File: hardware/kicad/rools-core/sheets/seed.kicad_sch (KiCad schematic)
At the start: 3 parts, among them J7 J_TOP_MAIN, J8 J_BOT_MAIN

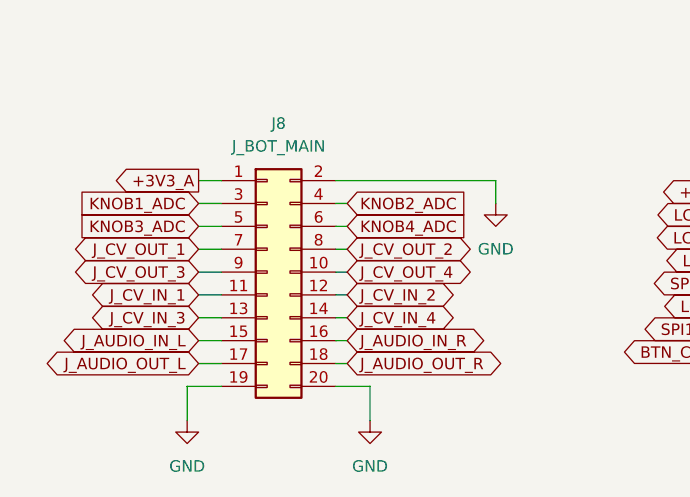
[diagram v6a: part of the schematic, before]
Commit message: Remove Patch reference assets and continue Core PCB routing.
Drop imported Patch symbols, local display footprint, and stale BOM CSV while advancing layout and schematic interconnects.

Co-authored-by: Cursor <cursoragent@cursor.com>
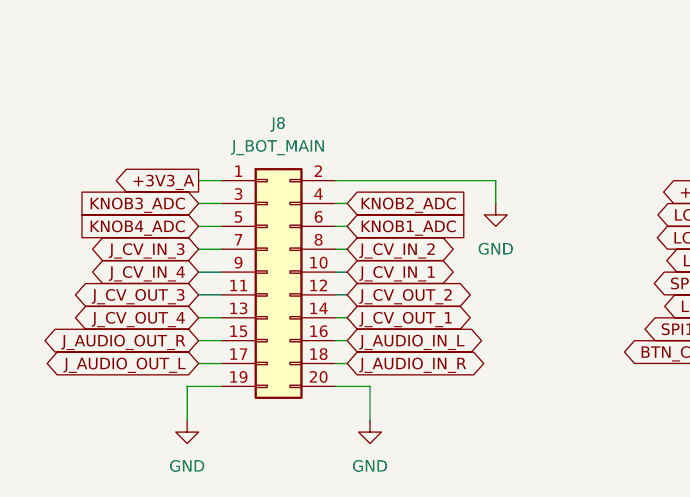
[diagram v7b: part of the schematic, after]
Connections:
- net J_AUDIO_IN_L: now also J8.16 (Pin_16); no longer J8.15 (Pin_15)
- net J_AUDIO_IN_R: now also J8.18 (Pin_18); no longer J8.16 (Pin_16)
- net J_AUDIO_OUT_R: now also J8.15 (Pin_15); no longer J8.18 (Pin_18)
- net J_CV_IN_1: now also J8.10 (Pin_10); no longer J8.11 (Pin_11)
- net J_CV_IN_2: now also J8.8 (Pin_8); no longer J8.12 (Pin_12)
- net J_CV_IN_3: now also J8.7 (Pin_7); no longer J8.13 (Pin_13)
- net J_CV_IN_4: now also J8.9 (Pin_9); no longer J8.14 (Pin_14)
- net J_CV_OUT_1: now also J8.14 (Pin_14); no longer J8.7 (Pin_7)
- net J_CV_OUT_2: now also J8.12 (Pin_12); no longer J8.8 (Pin_8)
- net J_CV_OUT_3: now also J8.11 (Pin_11); no longer J8.9 (Pin_9)
- net J_CV_OUT_4: now also J8.13 (Pin_13); no longer J8.10 (Pin_10)
- net KNOB1_ADC: now also J8.6 (Pin_6); no longer J8.3 (Pin_3)
- net KNOB3_ADC: now also J8.3 (Pin_3); no longer J8.5 (Pin_5)
- net KNOB4_ADC: now also J8.5 (Pin_5); no longer J8.6 (Pin_6)
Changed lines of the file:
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@@
 	(global_label "KNOB4_ADC"
 		(shape input)
-		(at 116.84 125.73 0)
-		(fields_autoplaced yes)
-		(effects
-			(font
-				(size 1.27 1.27)
-			)
-			(justify left)
-		)
-		(property "Intersheetrefs" "${INTERSHEET_REFS}"
-			(at 130.927 125.73 0)
-			(hide yes)
-			(show_name no)
-			(do_not_autoplace no)
-			(effects
-				(font
-					(size 1.27 1.27)
-				)
-				(justify left)
+		(at 100.33 125.73 180)
+		(fields_autoplaced yes)
+		(effects
+			(font
+				(size 1.27 1.27)
+			)
+			(justify right)
+		)
+		(property "Intersheetrefs" "${INTERSHEET_REFS}"
+			(at 86.243 125.73 0)
+			(hide yes)
+			(show_name no)
+			(do_not_autoplace no)
+			(effects
+				(font
+					(size 1.27 1.27)
+				)
+				(justify right)
 			)
 		)
@@
 	(global_label "J_AUDIO_IN_R"
 		(shape bidirectional)
-		(at 116.84 138.43 0)
-		(fields_autoplaced yes)
-		(effects
-			(font
-				(size 1.27 1.27)
-			)
-			(justify left)
-		)
-		(property "Intersheetrefs" "${INTERSHEET_REFS}"
-			(at 133.6364 138.43 0)
+		(at 116.84 140.97 0)
+		(fields_autoplaced yes)
+		(effects
+			(font
+				(size 1.27 1.27)
+			)
+			(justify left)
+		)
+		(property "Intersheetrefs" "${INTERSHEET_REFS}"
+			(at 133.6364 140.97 0)
 			(hide yes)
 			(show_name no)
@@
 	(global_label "J_CV_OUT_1"
 		(shape bidirectional)
-		(at 100.33 128.27 180)
-		(fields_autoplaced yes)
-		(effects
-			(font
-				(size 1.27 1.27)
-			)
-			(justify right)
-		)
-		(property "Intersheetrefs" "${INTERSHEET_REFS}"
-			(at 85.1666 128.27 0)
-			(hide yes)
-			(show_name no)
-			(do_not_autoplace no)
-			(effects
-				(font
-					(size 1.27 1.27)
-				)
-				(justify right)
+		(at 116.84 135.89 0)
+		(fields_autoplaced yes)
+		(effects
+			(font
+				(size 1.27 1.27)
+			)
+			(justify left)
+		)
+		(property "Intersheetrefs" "${INTERSHEET_REFS}"
+			(at 132.0034 135.89 0)
+			(hide yes)
+			(show_name no)
+			(do_not_autoplace no)
+			(effects
+				(font
+					(size 1.27 1.27)
+				)
+				(justify left)
 			)
 		)
@@
 	(global_label "J_CV_IN_1"
 		(shape bidirectional)
-		(at 100.33 133.35 180)
-		(fields_autoplaced yes)
-		(effects
-			(font
-				(size 1.27 1.27)
-			)
-			(justify right)
-		)
-		(property "Intersheetrefs" "${INTERSHEET_REFS}"
-			(at 86.8599 133.35 0)
-			(hide yes)
-			(show_name no)
-			(do_not_autoplace no)
-			(effects
-				(font
-					(size 1.27 1.27)
-				)
-				(justify right)
+		(at 116.84 130.81 0)
+		(fields_autoplaced yes)
+		(effects
+			(font
+				(size 1.27 1.27)
+			)
+			(justify left)
+		)
+		(property "Intersheetrefs" "${INTERSHEET_REFS}"
+			(at 130.3101 130.81 0)
+			(hide yes)
+			(show_name no)
+			(do_not_autoplace no)
+			(effects
+				(font
+					(size 1.27 1.27)
+				)
+				(justify left)
 			)
 		)
@@
 	(global_label "J_AUDIO_IN_L"
 		(shape bidirectional)
-		(at 100.33 138.43 180)
-		(fields_autoplaced yes)
-		(effects
-			(font
-				(size 1.27 1.27)
-			)
-			(justify right)
-		)
-		(property "Intersheetrefs" "${INTERSHEET_REFS}"
-			(at 83.7755 138.43 0)
-			(hide yes)
-			(show_name no)
-			(do_not_autoplace no)
-			(effects
-				(font
-					(size 1.27 1.27)
-				)
-				(justify right)
+		(at 116.84 138.43 0)
+		(fields_autoplaced yes)
+		(effects
+			(font
+				(size 1.27 1.27)
+			)
+			(justify left)
+		)
+		(property "Intersheetrefs" "${INTERSHEET_REFS}"
+			(at 133.3945 138.43 0)
+			(hide yes)
+			(show_name no)
+			(do_not_autoplace no)
+			(effects
+				(font
+					(size 1.27 1.27)
+				)
+				(justify left)
 			)
 		)
@@
 	(global_label "J_CV_IN_3"
 		(shape bidirectional)
-		(at 100.33 135.89 180)
-		(fields_autoplaced yes)
-		(effects
-			(font
-				(size 1.27 1.27)
-			)
-			(justify right)
-		)
-		(property "Intersheetrefs" "${INTERSHEET_REFS}"
-			(at 86.8599 135.89 0)
+		(at 100.33 128.27 180)
+		(fields_autoplaced yes)
+		(effects
+			(font
+				(size 1.27 1.27)
+			)
+			(justify right)
+		)
+		(property "Intersheetrefs" "${INTERSHEET_REFS}"
+			(at 86.8599 128.27 0)
 			(hide yes)
 			(show_name no)
@@
 	(global_label "J_CV_OUT_2"
 		(shape bidirectional)
-		(at 116.84 128.27 0)
-		(fields_autoplaced yes)
-		(effects
-			(font
-				(size 1.27 1.27)
-			)
-			(justify left)
-		)
-		(property "Intersheetrefs" "${INTERSHEET_REFS}"
-			(at 132.0034 128.27 0)
+		(at 116.84 133.35 0)
+		(fields_autoplaced yes)
+		(effects
+			(font
+				(size 1.27 1.27)
+			)
+			(justify left)
+		)
+		(property "Intersheetrefs" "${INTERSHEET_REFS}"
+			(at 132.0034 133.35 0)
 			(hide yes)
 			(show_name no)
@@
 	(global_label "J_CV_IN_2"
 		(shape bidirectional)
-		(at 116.84 133.35 0)
-		(fields_autoplaced yes)
-		(effects
-			(font
-				(size 1.27 1.27)
-			)
-			(justify left)
-		)
-		(property "Intersheetrefs" "${INTERSHEET_REFS}"
-			(at 130.3101 133.35 0)
+		(at 116.84 128.27 0)
+		(fields_autoplaced yes)
+		(effects
+			(font
+				(size 1.27 1.27)
+			)
+			(justify left)
+		)
+		(property "Intersheetrefs" "${INTERSHEET_REFS}"
+			(at 130.3101 128.27 0)
 			(hide yes)
 			(show_name no)
@@
 	(global_label "J_AUDIO_OUT_R"
 		(shape bidirectional)
-		(at 116.84 140.97 0)
-		(fields_autoplaced yes)
-		(effects
-			(font
-				(size 1.27 1.27)
-			)
-			(justify left)
-		)
-		(property "Intersheetrefs" "${INTERSHEET_REFS}"
-			(at 135.3297 140.97 0)
-			(hide yes)
-			(show_name no)
-			(do_not_autoplace no)
-			(effects
-				(font
-					(size 1.27 1.27)
-				)
-				(justify left)
+		(at 100.33 138.43 180)
+		(fields_autoplaced yes)
+		(effects
+			(font
+				(size 1.27 1.27)
+			)
+			(justify right)
+		)
+		(property "Intersheetrefs" "${INTERSHEET_REFS}"
+			(at 81.8403 138.43 0)
+			(hide yes)
+			(show_name no)
+			(do_not_autoplace no)
+			(effects
+				(font
+					(size 1.27 1.27)
+				)
+				(justify right)
 			)
 		)
@@
 	(global_label "KNOB3_ADC"
 		(shape input)
-		(at 100.33 125.73 180)
-		(fields_autoplaced yes)
-		(effects
-			(font
-				(size 1.27 1.27)
-			)
-			(justify right)
-		)
-		(property "Intersheetrefs" "${INTERSHEET_REFS}"
-			(at 86.243 125.73 0)
+		(at 100.33 123.19 180)
+		(fields_autoplaced yes)
+		(effects
+			(font
+				(size 1.27 1.27)
+			)
+			(justify right)
+		)
+		(property "Intersheetrefs" "${INTERSHEET_REFS}"
+			(at 86.243 123.19 0)
 			(hide yes)
 			(show_name no)
@@
 	(global_label "J_CV_OUT_4"
 		(shape bidirectional)
-		(at 116.84 130.81 0)
-		(fields_autoplaced yes)
-		(effects
-			(font
-				(size 1.27 1.27)
-			)
-			(justify left)
-		)
-		(property "Intersheetrefs" "${INTERSHEET_REFS}"
-			(at 132.0034 130.81 0)
-			(hide yes)
-			(show_name no)
-			(do_not_autoplace no)
-			(effects
-				(font
-					(size 1.27 1.27)
-				)
-				(justify left)
+		(at 100.33 135.89 180)
+		(fields_autoplaced yes)
+		(effects
+			(font
+				(size 1.27 1.27)
+			)
+			(justify right)
+		)
+		(property "Intersheetrefs" "${INTERSHEET_REFS}"
+			(at 85.1666 135.89 0)
+			(hide yes)
+			(show_name no)
+			(do_not_autoplace no)
+			(effects
+				(font
+					(size 1.27 1.27)
+				)
+				(justify right)
 			)
 		)
@@
 	(global_label "J_CV_IN_4"
 		(shape bidirectional)
-		(at 116.84 135.89 0)
-		(fields_autoplaced yes)
-		(effects
-			(font
-				(size 1.27 1.27)
-			)
-			(justify left)
-		)
-		(property "Intersheetrefs" "${INTERSHEET_REFS}"
-			(at 130.3101 135.89 0)
-			(hide yes)
-			(show_name no)
-			(do_not_autoplace no)
-			(effects
-				(font
-					(size 1.27 1.27)
-				)
-				(justify left)
+		(at 100.33 130.81 180)
+		(fields_autoplaced yes)
+		(effects
+			(font
+				(size 1.27 1.27)
+			)
+			(justify right)
+		)
+		(property "Intersheetrefs" "${INTERSHEET_REFS}"
+			(at 86.8599 130.81 0)
+			(hide yes)
+			(show_name no)
+			(do_not_autoplace no)
+			(effects
+				(font
+					(size 1.27 1.27)
+				)
+				(justify right)
 			)
 		)
@@
 	(global_label "KNOB1_ADC"
 		(shape input)
-		(at 100.33 123.19 180)
-		(fields_autoplaced yes)
-		(effects
-			(font
-				(size 1.27 1.27)
-			)
-			(justify right)
-		)
-		(property "Intersheetrefs" "${INTERSHEET_REFS}"
-			(at 86.243 123.19 0)
-			(hide yes)
-			(show_name no)
-			(do_not_autoplace no)
-			(effects
-				(font
-					(size 1.27 1.27)
-				)
-				(justify right)
+		(at 116.84 125.73 0)
+		(fields_autoplaced yes)
+		(effects
+			(font
+				(size 1.27 1.27)
+			)
+			(justify left)
+		)
+		(property "Intersheetrefs" "${INTERSHEET_REFS}"
+			(at 130.927 125.73 0)
+			(hide yes)
+			(show_name no)
+			(do_not_autoplace no)
+			(effects
+				(font
+					(size 1.27 1.27)
+				)
+				(justify left)
 			)
 		)
@@
 	(global_label "J_CV_OUT_3"
 		(shape bidirectional)
-		(at 100.33 130.81 180)
-		(fields_autoplaced yes)
-		(effects
-			(font
-				(size 1.27 1.27)
-			)
-			(justify right)
-		)
-		(property "Intersheetrefs" "${INTERSHEET_REFS}"
-			(at 85.1666 130.81 0)
-			(hide yes)
-			(show_name no)
+		(at 100.33 133.35 180)
+		(fields_autoplaced yes)
+		(effects
+			(font
+				(size 1.27 1.27)
+			)
+			(justify right)
+		)
+		(property "Intersheetrefs" "${INTERSHEET_REFS}"
+			(at 85.1666 133.35 0)
+			(hide yes)
+			(show_name no)

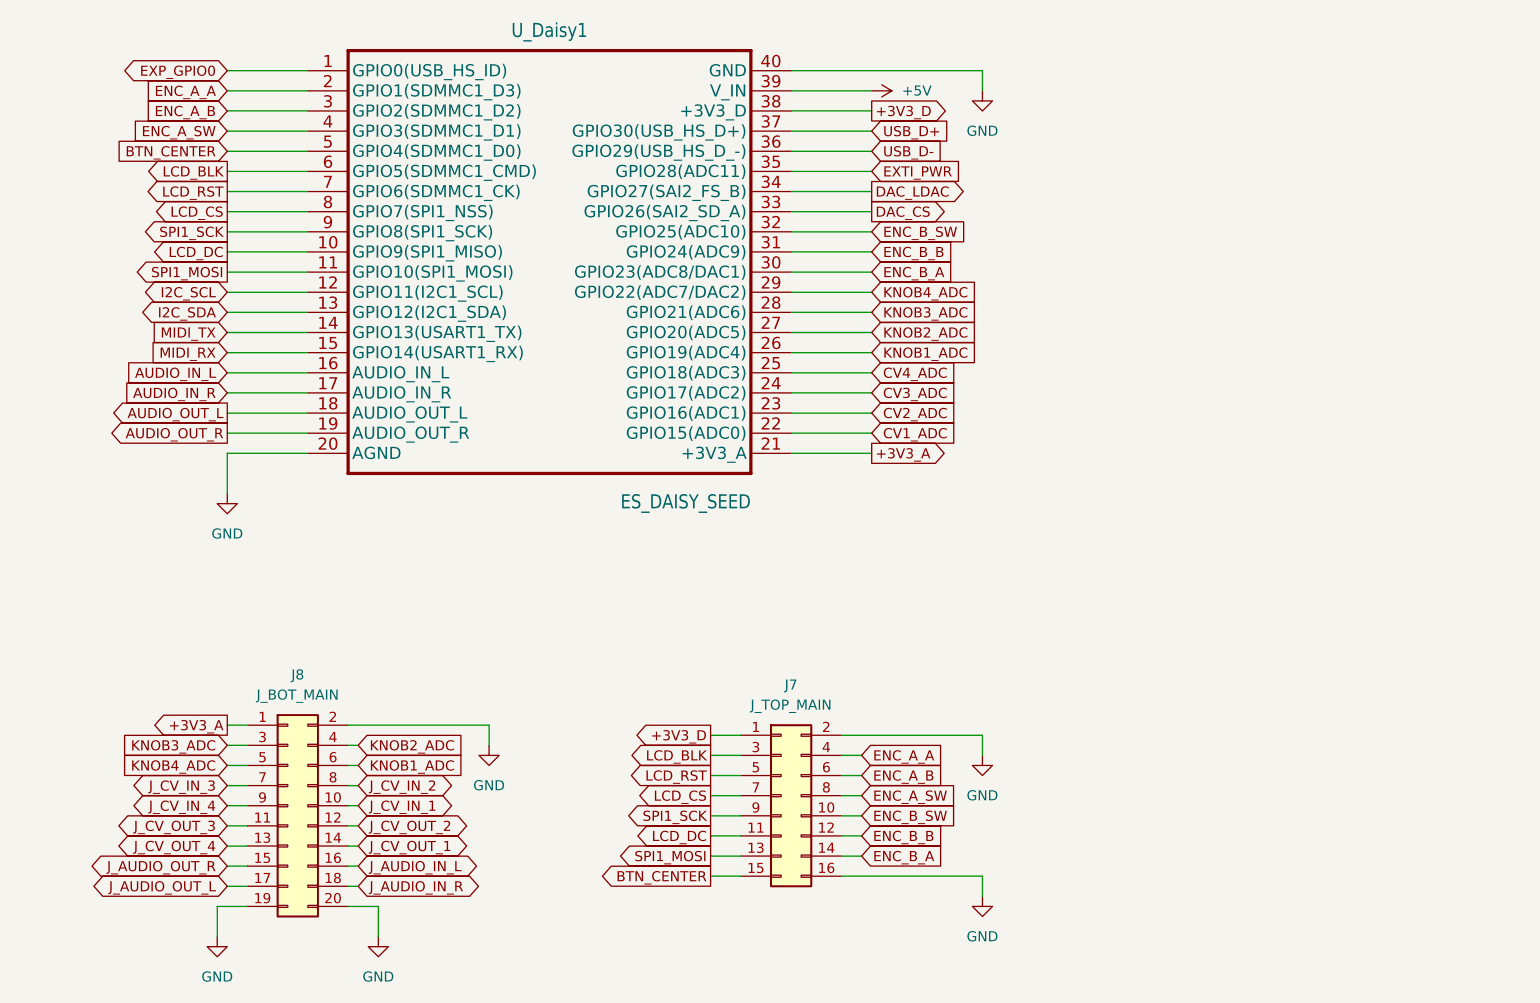
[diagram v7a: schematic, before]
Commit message: Align seed schematic with Electrosmith Daisy module footprint.
Update power and UI interconnects and continue Core PCB layout after removing the local footprint library.

Co-authored-by: Cursor <cursoragent@cursor.com>
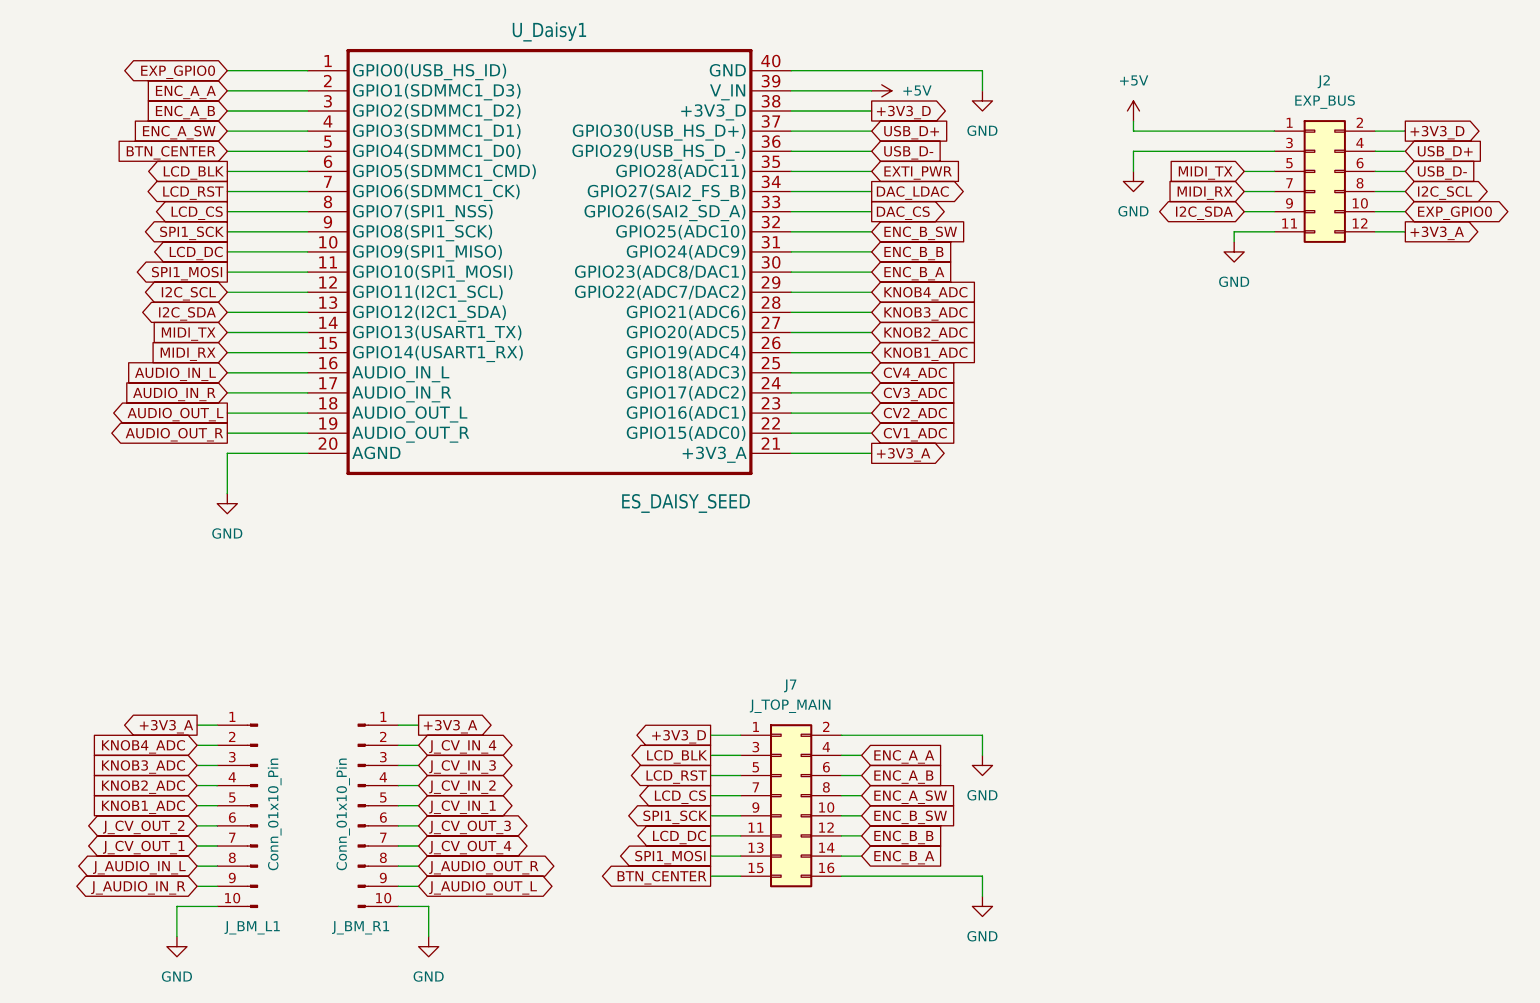
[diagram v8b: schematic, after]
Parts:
- removed J8: J_BOT_MAIN, Connector_PinSocket_2.54mm:PinSocket_2x10_P2.54mm_Vertical_SMD, symbol Connector_Generic:Conn_02x10_Odd_Even
- added J2: EXP_BUS, Connector_PinHeader_2.54mm:PinHeader_2x06_P2.54mm_Vertical, symbol Connector_Generic:Conn_02x06_Odd_Even
- added J_BM_L1: Conn_01x10_Pin, Connector_PinSocket_2.54mm:PinSocket_1x10_P2.54mm_Vertical, symbol Connector:Conn_01x10_Pin
- added J_BM_R1: Conn_01x10_Pin, Connector_PinSocket_2.54mm:PinSocket_1x11_P2.54mm_Vertical, symbol Connector:Conn_01x10_Pin
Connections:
- net +3V3_A: now also J2.12 (Pin_12), J_BM_L1.1 (Pin_1), J_BM_R1.1 (Pin_1)
- net +3V3_D: now also J2.2 (Pin_2)
- net +5V: now also J2.1 (Pin_1)
- net EXP_GPIO0: now also J2.10 (Pin_10)
- net GND: now also J2.11 (Pin_11), J2.3 (Pin_3), J_BM_L1.10 (Pin_10), J_BM_R1.10 (Pin_10)
- net I2C_SCL: now also J2.8 (Pin_8)
- net I2C_SDA: now also J2.9 (Pin_9)
- net J_AUDIO_IN_L: now also J_BM_L1.8 (Pin_8)
- net J_AUDIO_IN_R: now also J_BM_L1.9 (Pin_9)
- net J_AUDIO_OUT_L: now also J_BM_R1.9 (Pin_9)
- net J_AUDIO_OUT_R: now also J_BM_R1.8 (Pin_8)
- net J_CV_IN_1: now also J_BM_R1.5 (Pin_5)
- net J_CV_IN_2: now also J_BM_R1.4 (Pin_4)
- net J_CV_IN_3: now also J_BM_R1.3 (Pin_3)
- net J_CV_IN_4: now also J_BM_R1.2 (Pin_2)
- net J_CV_OUT_1: now also J_BM_L1.7 (Pin_7)
- net J_CV_OUT_2: now also J_BM_L1.6 (Pin_6)
- net J_CV_OUT_3: now also J_BM_R1.6 (Pin_6)
- net J_CV_OUT_4: now also J_BM_R1.7 (Pin_7)
- net KNOB1_ADC: now also J_BM_L1.5 (Pin_5)
- net KNOB2_ADC: now also J_BM_L1.4 (Pin_4)
- net KNOB3_ADC: now also J_BM_L1.3 (Pin_3)
- net KNOB4_ADC: now also J_BM_L1.2 (Pin_2)
- net MIDI_RX: now also J2.7 (Pin_7)
- net MIDI_TX: now also J2.5 (Pin_5)
- net USB_D+: now also J2.4 (Pin_4)
- net USB_D-: now also J2.6 (Pin_6)
